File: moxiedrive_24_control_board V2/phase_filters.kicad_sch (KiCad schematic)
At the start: 24 parts, among them Q801 30v 100ma, Q802 30v 100ma, Q803 30v 100ma, Q804 30v 100ma, Q805 30v 100ma, Q806 30v 100ma

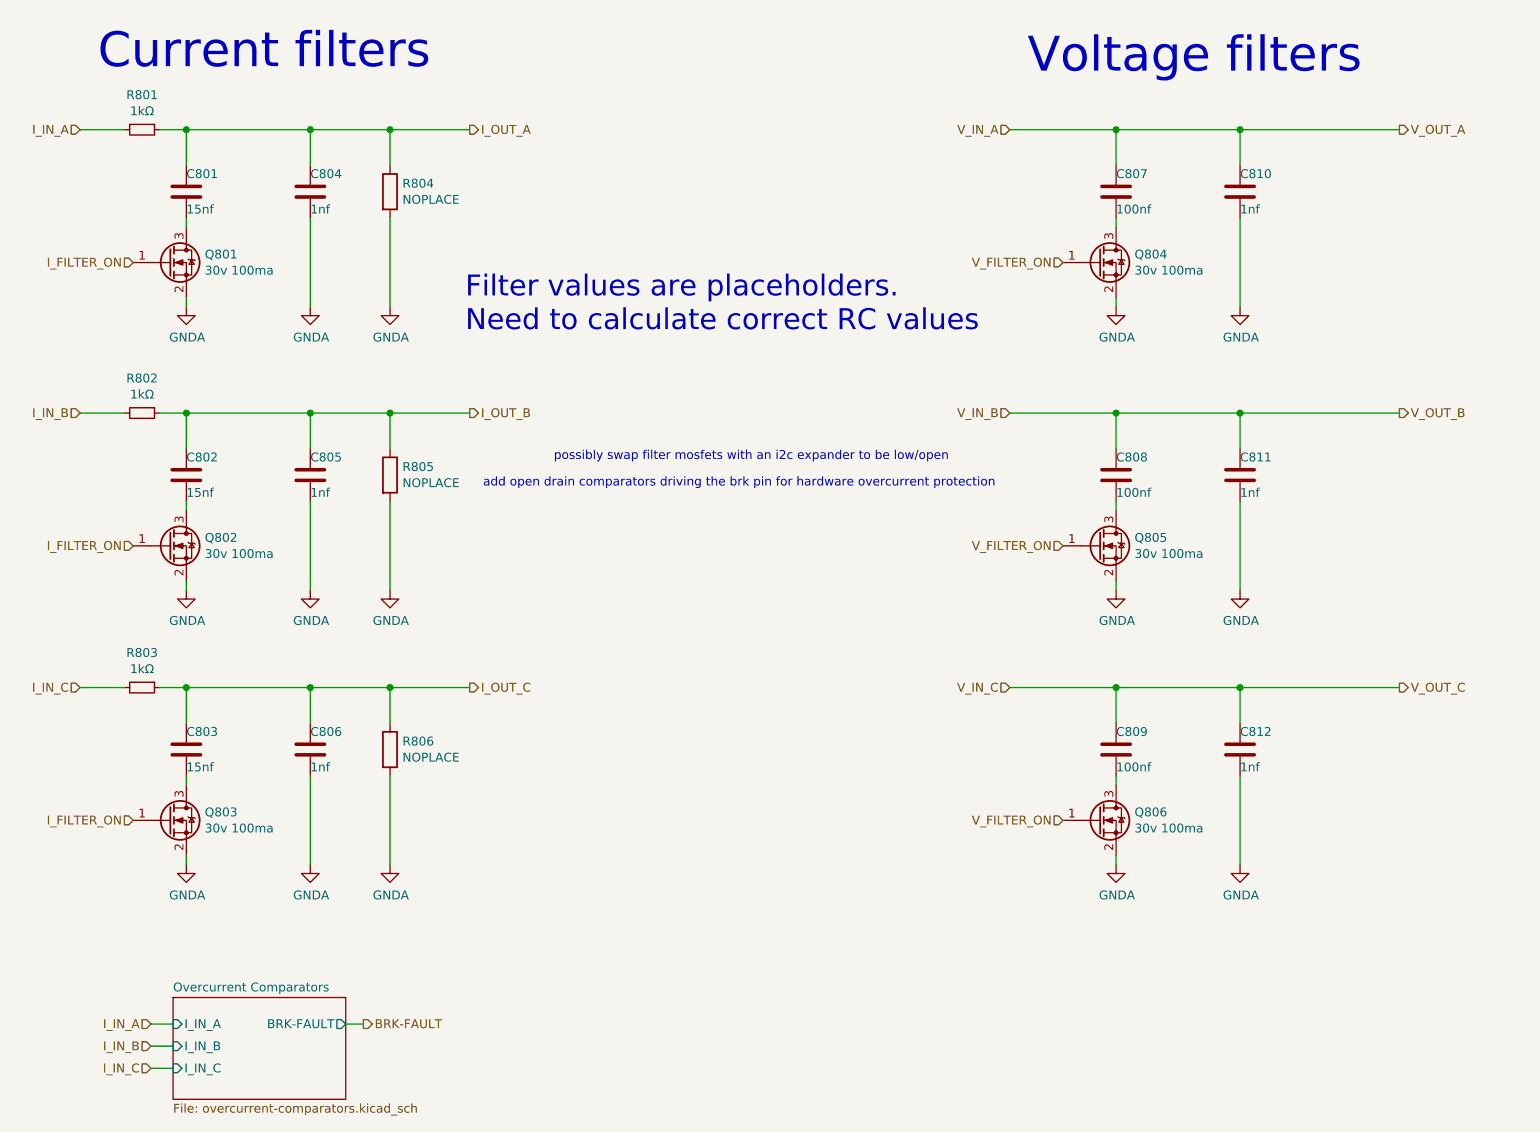
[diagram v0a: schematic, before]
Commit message: fix misplaced component
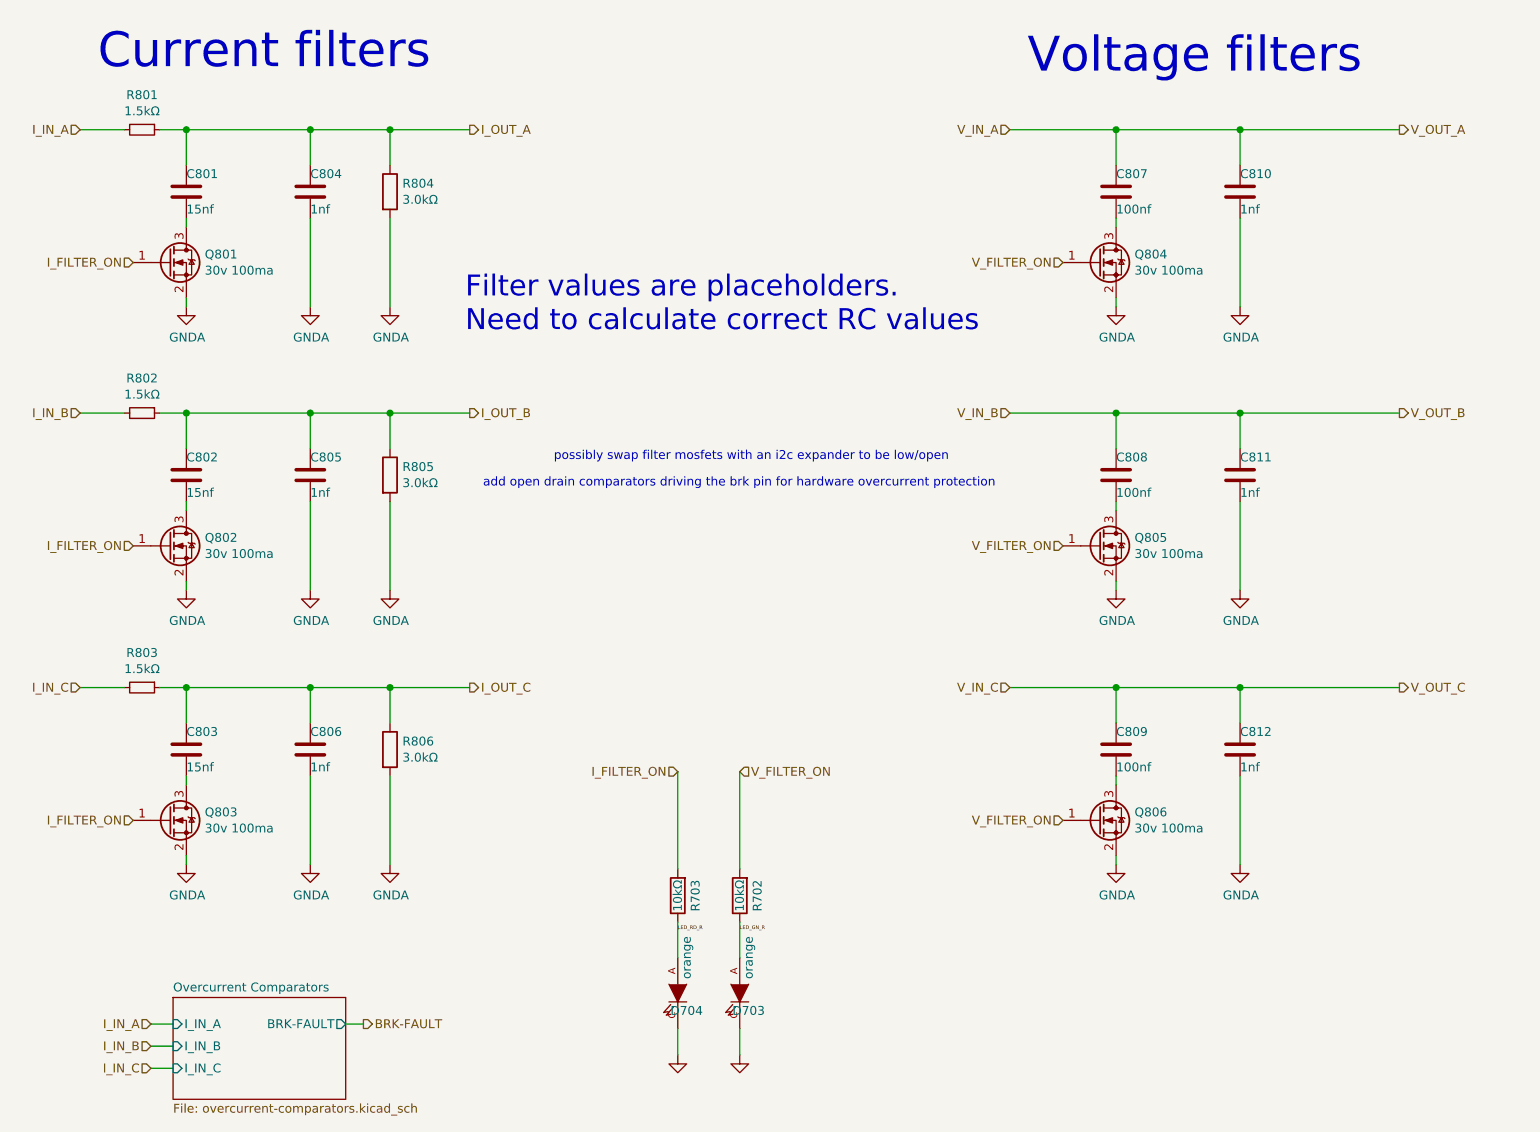
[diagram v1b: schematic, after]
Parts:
- added D703, D704: orange, pkl_dipol:D_0603, symbol 24_control_board-rescue:pkl_LED-pkl_device
- added R702, R703: 10kΩ, pkl_dipol:R_0402, symbol 24_control_board-rescue:R-Device-MoxiE_Control_board-rescue
- R801, R802, R803: value 1kΩ -> 1.5kΩ
- R804, R805, R806: value NOPLACE -> 3.0kΩ
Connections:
- net I_FILTER_ON: now also R703.2
- net V_FILTER_ON: now also R702.2
- new net GND: D703.C, D704.C
- new net LED_GN_R: D703.A, R702.1
- new net LED_RD_R: D704.A, R703.1
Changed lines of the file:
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@@
+    (stroke (width 0) (type solid))
+  )
+  (wire (pts (xy 140.335 172.085) (xy 140.335 168.275))
     (stroke (width 0) (type solid))
   )
@@
   )
   (wire (pts (xy 87.63 144.78) (xy 87.63 132.08))
+    (stroke (width 0) (type solid))
+  )
+  (wire (pts (xy 140.335 158.115) (xy 140.335 153.035))
     (stroke (width 0) (type solid))
   )
@@
     (stroke (width 0) (type default))
   )
+  (wire (pts (xy 149.225 158.115) (xy 149.225 153.035))
+    (stroke (width 0) (type solid))
+  )
   (wire (pts (xy 203.2 39.37) (xy 203.2 44.45))
     (stroke (width 0) (type solid))
@@
     (stroke (width 0) (type solid))
   )
+  (wire (pts (xy 149.225 172.085) (xy 149.225 168.275))
+    (stroke (width 0) (type solid))
+  )
   (wire (pts (xy 66.04 119.38) (xy 69.85 119.38))
     (stroke (width 0) (type solid))
@@
   )
   (wire (pts (xy 203.2 80.01) (xy 203.2 85.09))
+    (stroke (width 0) (type solid))
+  )
+  (wire (pts (xy 149.225 131.445) (xy 149.225 145.415))
+    (stroke (width 0) (type solid))
+  )
+  (wire (pts (xy 140.335 145.415) (xy 140.335 131.445))
     (stroke (width 0) (type solid))
   )
@@
     (effects (font (size 3 3)) (justify left bottom))
   )
+  (label "LED_RD_R" (at 140.335 154.305 0) (fields_autoplaced)
+    (effects (font (size 0.508 0.508)) (justify left bottom))
+  )
+  (label "LED_GN_R" (at 149.225 154.305 0) (fields_autoplaced)
+    (effects (font (size 0.508 0.508)) (justify left bottom))
+  )
+  (hierarchical_label "V_FILTER_ON" (shape input) (at 149.225 131.445 0) (fields_autoplaced)
+    (effects (font (size 1.27 1.27)) (justify left))
+  )
   (hierarchical_label "V_OUT_B" (shape output) (at 243.84 80.01 0) (fields_autoplaced)
     (effects (font (size 1.27 1.27)) (justify left))
@@
     (effects (font (size 1.27 1.27)) (justify right))
   )
+  (hierarchical_label "I_FILTER_ON" (shape input) (at 140.335 131.445 180) (fields_autoplaced)
+    (effects (font (size 1.27 1.27)) (justify right))
+  )
   (hierarchical_label "I_IN_A" (shape input) (at 64.77 167.64 180) (fields_autoplaced)
     (effects (font (size 1.27 1.27)) (justify right))
@@
       (effects (font (size 1.27 1.27)))
     )
-    (property "Value" "1kΩ" (at 63.5 36.703 90)
+    (property "Value" "1.5kΩ" (at 63.5 36.703 90)
       (effects (font (size 1.27 1.27)))
     )
@@
       (effects (font (size 1.27 1.27)))
     )
-    (property "Value" "1kΩ" (at 63.5 77.343 90)
+    (property "Value" "1.5kΩ" (at 63.5 77.343 90)
       (effects (font (size 1.27 1.27)))
     )
@@
       (effects (font (size 1.27 1.27)))
     )
-    (property "Value" "1kΩ" (at 63.5 116.713 90)
+    (property "Value" "1.5kΩ" (at 63.5 116.713 90)
       (effects (font (size 1.27 1.27)))
     )
@@
       (effects (font (size 1.27 1.27)) (justify left))
     )
-    (property "Value" "NOPLACE" (at 100.838 90.043 0)
+    (property "Value" "3.0kΩ" (at 100.838 90.043 0)
       (effects (font (size 1.27 1.27)) (justify left))
     )
@@
       (effects (font (size 1.27 1.27)) (justify left))
     )
-    (property "Value" "NOPLACE" (at 100.838 129.413 0)
+    (property "Value" "3.0kΩ" (at 100.838 129.413 0)
       (effects (font (size 1.27 1.27)) (justify left))
     )
@@
       (effects (font (size 1.27 1.27)) (justify left))
     )
-    (property "Value" "NOPLACE" (at 100.838 49.403 0)
+    (property "Value" "3.0kΩ" (at 100.838 49.403 0)
       (effects (font (size 1.27 1.27)) (justify left))
     )
@@
     )
   )
+  (symbol (lib_id "24_control_board-rescue:R-Device-MoxiE_Control_board-rescue") (at 149.225 149.225 180) (unit 1)
+    (in_bom yes) (on_board yes) (dnp no)
+    (property "Reference" "R702" (at 151.765 149.225 90)
+      (effects (font (size 1.27 1.27)))
+    )
+    (property "Value" "10kΩ" (at 149.225 149.225 90)
+      (effects (font (size 1.27 1.27)))
+    )
+    (property "Footprint" "pkl_dipol:R_0402" (at 149.225 149.225 0)
+      (effects (font (size 1.524 1.524)) hide)
+    )
+    (property "Datasheet" "" (at 149.225 149.225 0)
+      (effects (font (size 1.524 1.524)) hide)
+    )
+    (pin "1")
+    (pin "2")
+    (instances
+      (project "24_control_board"
+        (path "/3857af76-7e47-49fe-84f3-3378f0b9a08d/00000000-0000-0000-0000-00005b397924"
+          (reference "R702") (unit 1)
+        )
+        (path "/3857af76-7e47-49fe-84f3-3378f0b9a08d/00000000-0000-0000-0000-00005efd8fb1"
+          (reference "R1") (unit 1)
+        )
+      )
+    )
+  )
   (symbol (lib_id "Device:C") (at 203.2 88.9 0) (unit 1)
     (in_bom yes) (on_board yes) (dnp no)
@@
     )
   )
+  (symbol (lib_id "24_control_board-rescue:pkl_LED-pkl_device") (at 140.335 163.195 270) (unit 1)
+    (in_bom yes) (on_board yes) (dnp no)
+    (property "Reference" "D704" (at 141.605 165.735 90)
+      (effects (font (size 1.27 1.27)))
+    )
+    (property "Value" "orange" (at 141.605 158.115 0)
+      (effects (font (size 1.27 1.27)))
+    )
+    (property "Footprint" "pkl_dipol:D_0603" (at 140.335 163.195 0)
+      (effects (font (size 1.524 1.524)) hide)
+    )
+    (property "Datasheet" "" (at 140.335 163.195 0)
+      (effects (font (size 1.524 1.524)) hide)
+    )
+    (pin "A")
+    (pin "C")
+    (instances
+      (project "24_control_board"
+        (path "/3857af76-7e47-49fe-84f3-3378f0b9a08d/00000000-0000-0000-0000-00005b397924"
+          (reference "D704") (unit 1)
+        )
+        (path "/3857af76-7e47-49fe-84f3-3378f0b9a08d/00000000-0000-0000-0000-00005efd8fb1"
+          (reference "D2") (unit 1)
+        )
+      )
+    )
+  )
+  (symbol (lib_id "24_control_board-rescue:R-Device-MoxiE_Control_board-rescue") (at 140.335 149.225 180) (unit 1)
+    (in_bom yes) (on_board yes) (dnp no)
+    (property "Reference" "R703" (at 142.875 149.225 90)
+      (effects (font (size 1.27 1.27)))
+    )
+    (property "Value" "10kΩ" (at 140.335 149.225 90)
+      (effects (font (size 1.27 1.27)))
+    )
+    (property "Footprint" "pkl_dipol:R_0402" (at 140.335 149.225 0)
+      (effects (font (size 1.524 1.524)) hide)
+    )
+    (property "Datasheet" "" (at 140.335 149.225 0)
+      (effects (font (size 1.524 1.524)) hide)
+    )
+    (pin "1")
+    (pin "2")
+    (instances
+      (project "24_control_board"
+        (path "/3857af76-7e47-49fe-84f3-3378f0b9a08d/00000000-0000-0000-0000-00005b397924"
+          (reference "R703") (unit 1)
+        )
+        (path "/3857af76-7e47-49fe-84f3-3378f0b9a08d/00000000-0000-0000-0000-00005efd8fb1"
+          (reference "R2") (unit 1)
+        )
+      )
+    )
+  )
   (symbol (lib_id "Device:Q_NMOS_GSD") (at 200.66 138.43 0) (unit 1)
     (in_bom yes) (on_board yes) (dnp no)
@@
     )
   )
+  (symbol (lib_id "24_control_board-rescue:GND-power-MoxiE_Control_board-rescue") (at 140.335 172.085 0) (unit 1)
+    (in_bom yes) (on_board yes) (dnp no)
+    (property "Reference" "#PWR0705" (at 140.335 172.085 0)
+      (effects (font (size 0.762 0.762)) hide)
+    )
+    (property "Value" "GND" (at 140.335 173.863 0)
+      (effects (font (size 0.762 0.762)) hide)
+    )
+    (property "Footprint" "" (at 140.335 172.085 0)
+      (effects (font (size 1.524 1.524)) hide)
+    )
+    (property "Datasheet" "" (at 140.335 172.085 0)
+      (effects (font (size 1.524 1.524)) hide)
+    )
+    (pin "1")
+    (instances
+      (project "24_control_board"
+        (path "/3857af76-7e47-49fe-84f3-3378f0b9a08d/00000000-0000-0000-0000-00005b397924"
+          (reference "#PWR0705") (unit 1)
+        )
+        (path "/3857af76-7e47-49fe-84f3-3378f0b9a08d/00000000-0000-0000-0000-00005efd8fb1"
+          (reference "#PWR02") (unit 1)
+        )
+      )
+    )
+  )
   (symbol (lib_id "Device:C") (at 220.98 128.27 0) (unit 1)
     (in_bom yes) (on_board yes) (dnp no)
@@
     )
   )
+  (symbol (lib_id "24_control_board-rescue:pkl_LED-pkl_device") (at 149.225 163.195 270) (unit 1)
+    (in_bom yes) (on_board yes) (dnp no)
+    (property "Reference" "D703" (at 150.495 165.735 90)
+      (effects (font (size 1.27 1.27)))
+    )
+    (property "Value" "orange" (at 150.495 158.115 0)
+      (effects (font (size 1.27 1.27)))
+    )
+    (property "Footprint" "pkl_dipol:D_0603" (at 149.225 163.195 0)
+      (effects (font (size 1.524 1.524)) hide)
+    )
+    (property "Datasheet" "" (at 149.225 163.195 0)
+      (effects (font (size 1.524 1.524)) hide)
+    )
+    (pin "A")
+    (pin "C")
+    (instances
+      (project "24_control_board"
+        (path "/3857af76-7e47-49fe-84f3-3378f0b9a08d/00000000-0000-0000-0000-00005b397924"
+          (reference "D703") (unit 1)
+        )
+        (path "/3857af76-7e47-49fe-84f3-3378f0b9a08d/00000000-0000-0000-0000-00005efd8fb1"
+          (reference "D1") (unit 1)
+        )
+      )
+    )
+  )
   (symbol (lib_id "Device:C") (at 220.98 48.26 0) (unit 1)
     (in_bom yes) (on_board yes) (dnp no)
@@
         )
       )
+    )
+  )
+  (symbol (lib_id "24_control_board-rescue:GND-power-MoxiE_Control_board-rescue") (at 149.225 172.085 0) (unit 1)
+    (in_bom yes) (on_board yes) (dnp no)
+    (property "Reference" "#PWR0704" (at 149.225 172.085 0)
+      (effects (font (size 0.762 0.762)) hide)
+    )
+    (property "Value" "GND" (at 149.225 173.863 0)
+      (effects (font (size 0.762 0.762)) hide)
+    )
+    (property "Footprint" "" (at 149.225 172.085 0)
+      (effects (font (size 1.524 1.524)) hide)
+    )
+    (property "Datasheet" "" (at 149.225 172.085 0)
+      (effects (font (size 1.524 1.524)) hide)
+    )
+    (pin "1")
+    (instances
+      (project "24_control_board"
+        (path "/3857af76-7e47-49fe-84f3-3378f0b9a08d/00000000-0000-0000-0000-00005b397924"
+          (reference "#PWR0704") (unit 1)
+        )
+        (path "/3857af76-7e47-49fe-84f3-3378f0b9a08d/00000000-0000-0000-0000-00005efd8fb1"
+          (reference "#PWR01") (unit 1)
+        )
+      )
